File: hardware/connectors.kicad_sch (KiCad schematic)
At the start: 4 parts, among them J1 74650073R, J4 Conn_01x06, J5 UMPT-08-01-L-RA-WT-P-TR, J8 UMPT-08-01-L-RA-WT-P-TR

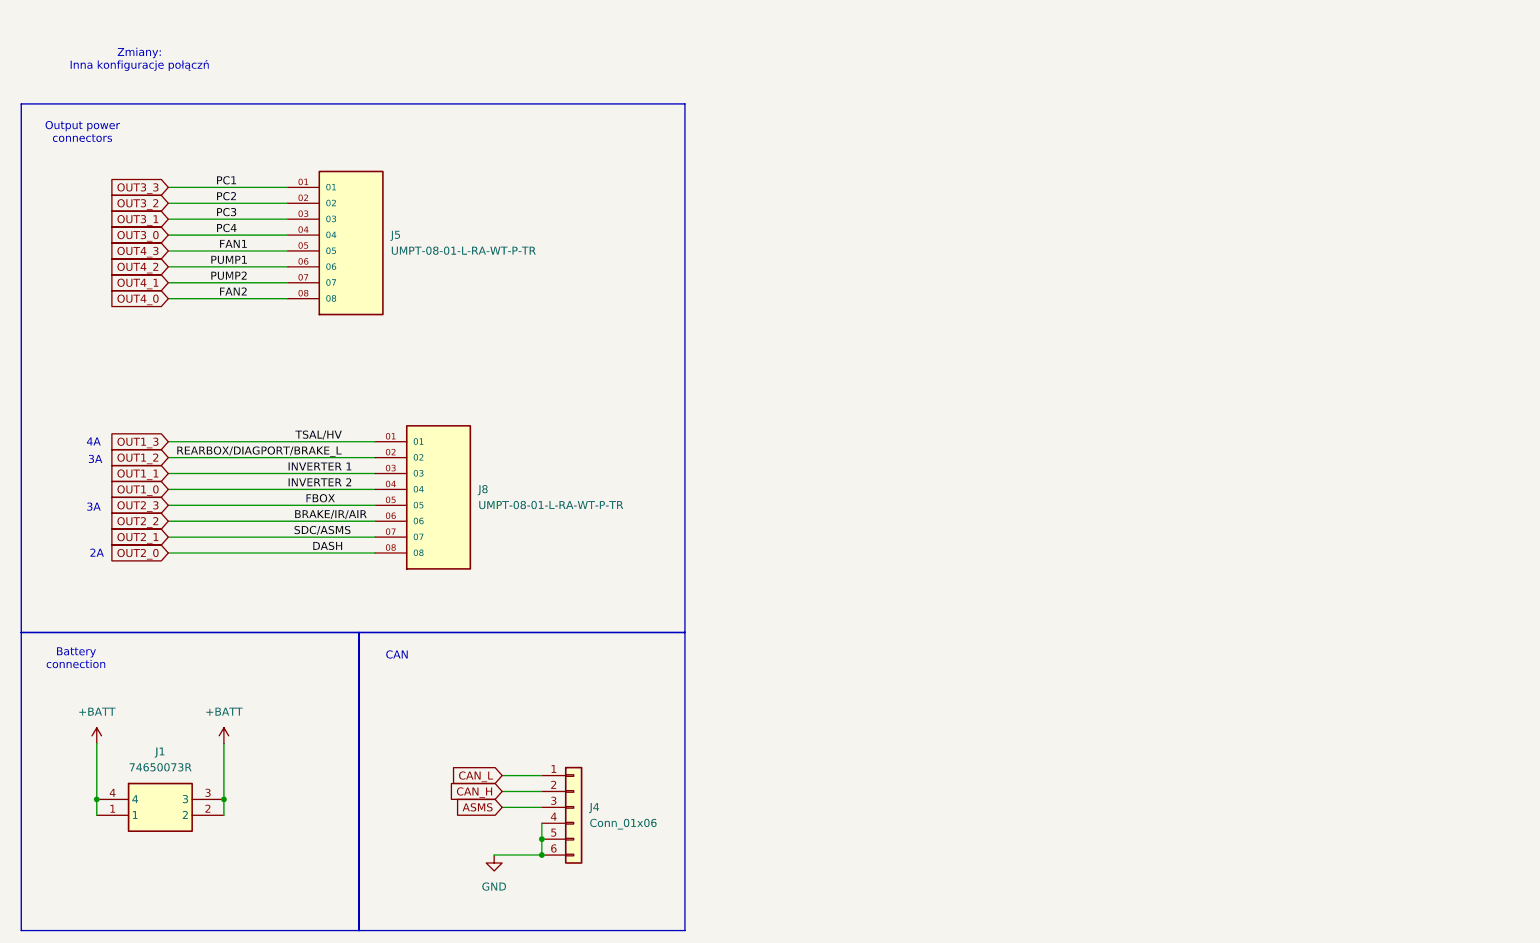
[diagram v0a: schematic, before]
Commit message: Changed CAN to isolated and added a new board-to-board plug
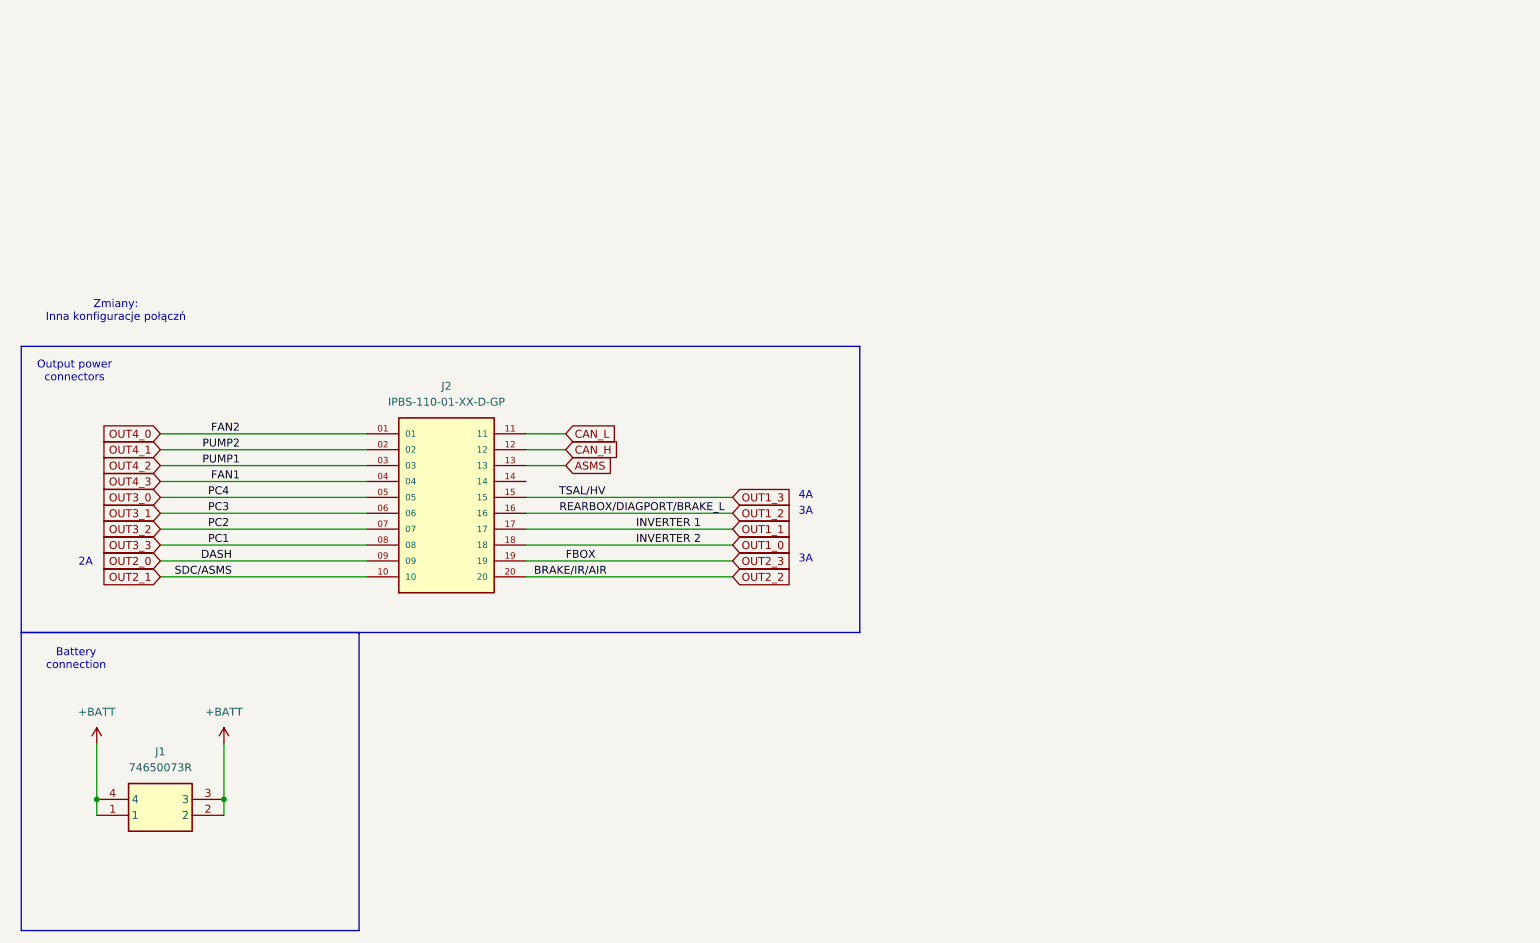
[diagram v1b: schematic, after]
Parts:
- removed J4: Conn_01x06, Connector_IDC:IDC-Header_2x03_P2.54mm_Vertical, symbol Connector_Generic:Conn_01x06
- removed J5, J8: UMPT-08-01-L-RA-WT-P-TR, UMPT-08-01-L-RA-WT-P-TR:SAMTEC_UMPT-08-01-L-RA-WT-P-TR, symbol UMPT-08-01-L-RA-WT-P-TR:UMPT-08-01-L-RA-WT-P-TR
- added J2: IPBS-110-01-XX-D-GP, IPBS-110-01-T-D-GP:SAMTEC_IPBS-110-01-XX-D-GP, symbol IPBS-110-01-XX-D-GP:IPBS-110-01-XX-D-GP
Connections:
- net ASMS: now also J2.13
- net CAN_H: now also J2.12
- net CAN_L: now also J2.11
- net OUT1_0: now also J2.18
- net OUT1_1: now also J2.17
- net OUT1_2: now also J2.16
- net OUT1_3: now also J2.15
- net OUT2_0: now also J2.09
- net OUT2_1: now also J2.10
- net OUT2_2: now also J2.20
- net OUT2_3: now also J2.19
- net OUT3_0: now also J2.05
- net OUT3_1: now also J2.06
- net OUT3_2: now also J2.07
- net OUT3_3: now also J2.08
- net OUT4_0: now also J2.01
- net OUT4_1: now also J2.02
- net OUT4_2: now also J2.03
- net OUT4_3: now also J2.04
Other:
- note removed: "CAN"

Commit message: NEW SCHEMATIC
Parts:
- added C28: 10n, Capacitor_SMD:C_0603_1608Metric_Pad1.08x0.95mm_HandSolder, symbol Device:C_Small
- added D10: PESD5V0L2BT,215, Package_TO_SOT_SMD:SOT-23-3, symbol Device:D_TVS_Dual_AAC
- added D11: SP0505BAHTG, Package_TO_SOT_SMD:SOT-23-6_Handsoldering, symbol Power_Protection:SP0505BAHT
- added J3: FTSH-107-01-L-D-K, PDM:FTSH-107-XX-YYY-D-K, symbol PDM:FTSH-107-01-L-D-K
- added J4: USB_C_Receptacle_USB2.0_14P, Connector_USB:USB_C_Receptacle_JAE_DX07S024WJ3R400, symbol Connector:USB_C_Receptacle_USB2.0_14P
- added R14, R15: 5k1, Resistor_SMD:R_0603_1608Metric_Pad0.98x0.95mm_HandSolder, symbol Device:R_Small
- added U5: TPD2E2U06DCK, Package_TO_SOT_SMD:SOT-323_SC-70, symbol Power_Protection:TPD2E2U06DCK
- J1: footprint 74650073R -> PDM:74650073R; symbol Redcube_conn:74650073R -> PDM:74650073R; Done? (none) -> y
- J2: footprint IPBS-110-01-T-D-GP:SAMTEC_IPBS-110-01-XX-D-GP -> PDM:IPBS11001TDGP; symbol IPBS-110-01-XX-D-GP:IPBS-110-01-XX-D-GP -> PDM:IPBS-110-01-T-D-GP; Done? (none) -> y; Manufacturer_Name (none) -> SAMTEC; Manufacturer_Part_Number (none) -> IPBS-110-01-T-D-GP; Mouser Part Number (none) -> 200-IPBS11001TDGP; Mouser Price/Stock (none) -> https://www.mouser.co.uk/ProductDetail/Samtec/IPBS-110-01-T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
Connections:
- net OUT1_0: now also J2.9; no longer J2.18
- net OUT1_1: now also J2.10; no longer J2.17
- net OUT1_2: now also J2.20; no longer J2.16
- net OUT1_3: now also J2.19; no longer J2.15
- net OUT2_0: now also J2.5; no longer J2.09
- net OUT2_1: now also J2.6; no longer J2.10
- net OUT2_2: now also J2.7; no longer J2.20
- net OUT2_3: now also J2.8; no longer J2.19
- net OUT3_0: now also J2.1; no longer J2.05
- net OUT3_1: now also J2.2; no longer J2.06
- net OUT3_2: now also J2.3; no longer J2.07
- net OUT3_3: now also J2.4; no longer J2.08
- net CAN_H renamed CAN.P
- net CAN.P: now also D10.2 (A2)
- net CAN_L renamed CAN.N
- net CAN.N: now also D10.1 (A1)
- removed net OUT4_0: J2.01
- removed net OUT4_1: J2.02
- removed net OUT4_2: J2.03
- removed net OUT4_3: J2.04
- new net: J4.B5 (CC2), R15.2
- new net: J4.A5 (CC1), R14.2
- new net: C28.1, J4.S1 (SHIELD)
- new net +3V3: J3.3
- new net CAN_GND_ISO: D10.3 (common)
- new net GND: C28.2, D11.2 (A), J3.11, J3.5, J3.7, J4.A1 (GND), J4.A12 (GND), J4.B1 (GND), J4.B12 (GND), R14.1, R15.1, U5.3
- new net OUT0_0: J2.18
- new net OUT0_1: J2.17
- new net OUT0_2: J2.16
- new net OUT0_3: J2.15
- new net RST: D11.4 (K), J3.12
- new net SW.CLK: D11.6 (K), J3.6
- new net SW.DIO: D11.5 (K), J3.4
- new net USART.RX: D11.1 (K), J3.13
- new net USART.TX: D11.3 (K), J3.14
- new net USB.+: J4.A6 (D+), J4.B6 (D+), U5.2
- new net USB.-: J4.A7 (D-), J4.B7 (D-), U5.1
- new net VBUS: J4.A4 (VBUS), J4.A9 (VBUS), J4.B4 (VBUS), J4.B9 (VBUS)
- no-connect marks 0 -> 6
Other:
- note added: "BATTERY CONNECTOR"
- note added: "Changes: New connection layout"
- note added: "ESD CAN PROTECTION"
- note added: "ESD PROGRAMMER PROTECTION"
- note added: "ESD USB PROTECTION"
- note added: "OUTPUT POWER CONNECTOR"
- note added: "PROGRAMMER"
- note added: "USB C"
- note removed: "Battery connection"
- note removed: "Output power connectors"
- note removed: "Zmiany: Inna konfiguracje połączń"
- company: (none) -> Authors: Grzegorz Potocki Jędrzej Kasprzyk
- title: (none) -> PDUv3
- moved on the sheet: J1, J2

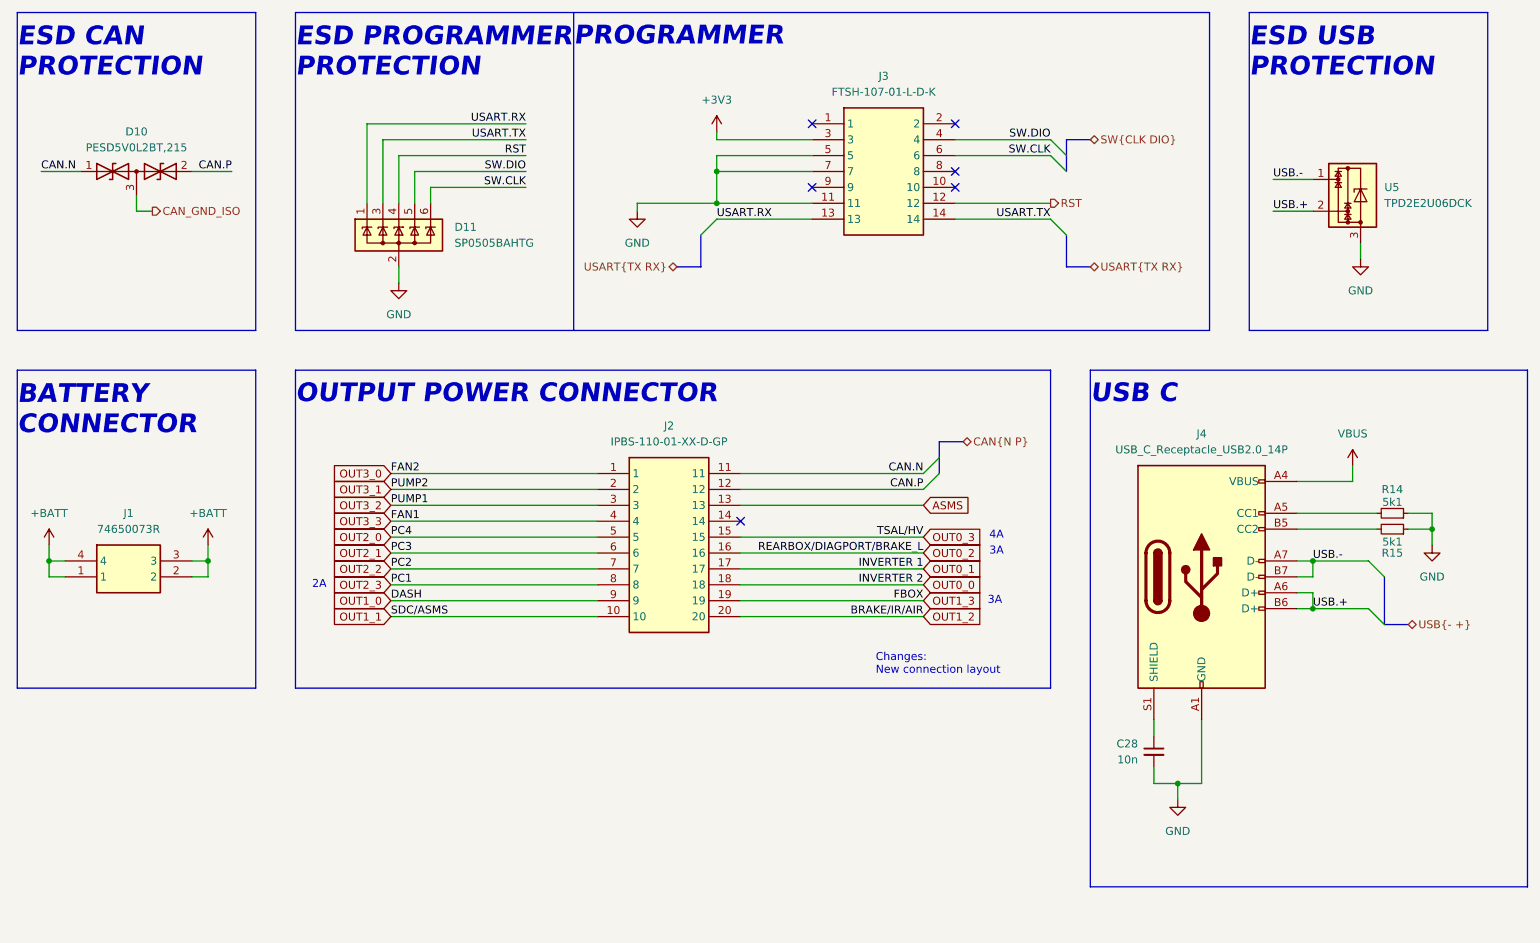
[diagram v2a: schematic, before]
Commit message: new pcb layout & can coppied from steeringwheel
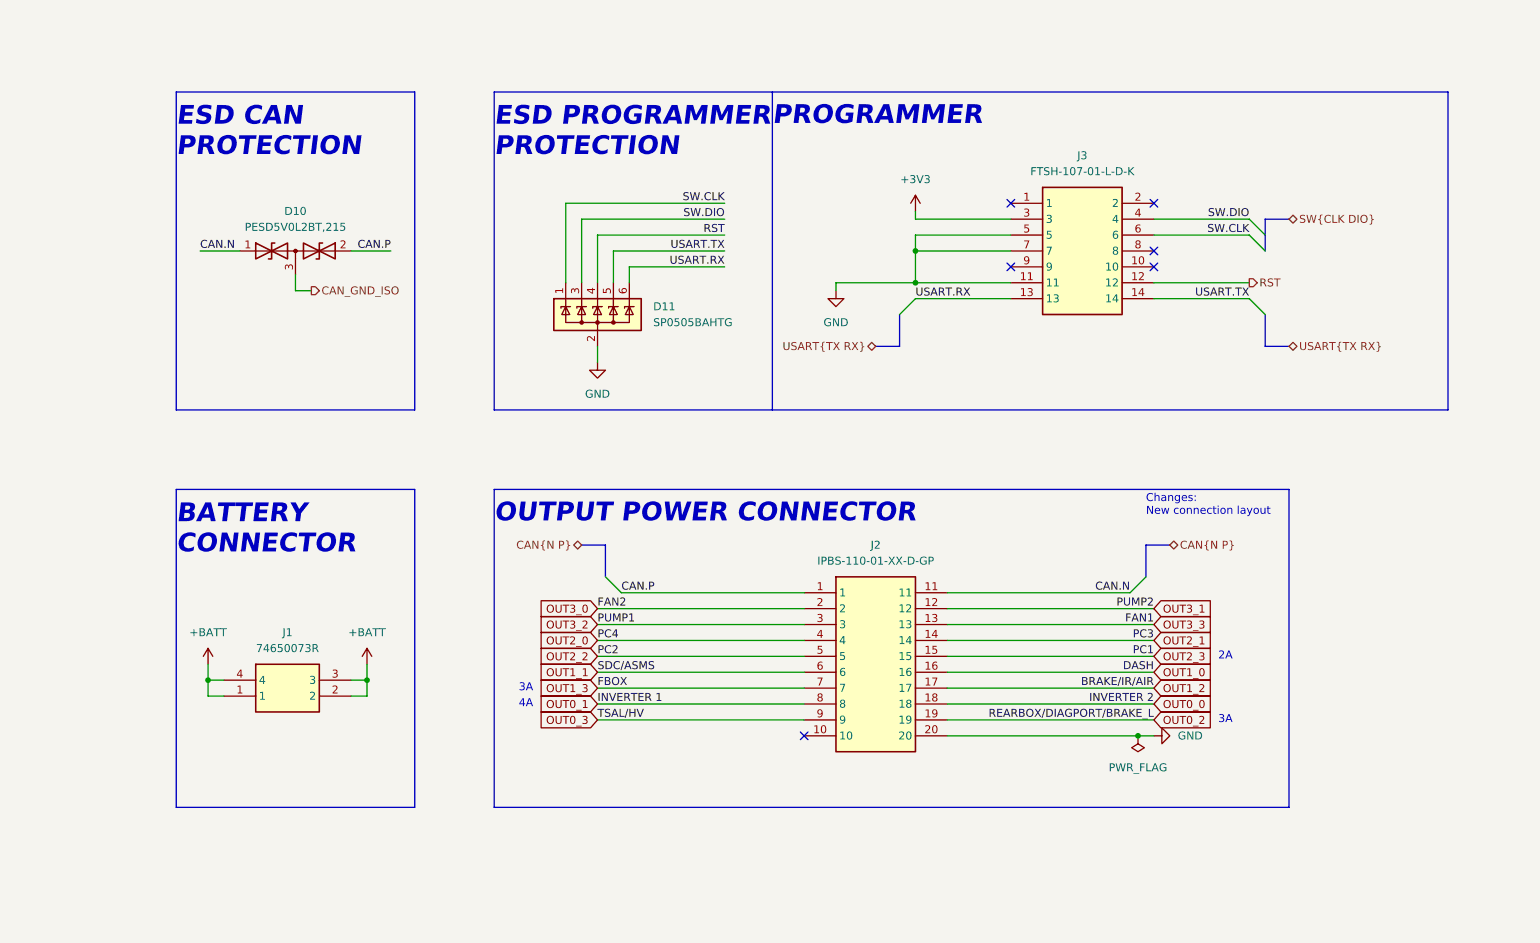
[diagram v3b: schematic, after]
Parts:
- removed C28: 10n, Capacitor_SMD:C_0603_1608Metric_Pad1.08x0.95mm_HandSolder, symbol Device:C_Small
- removed J4: USB_C_Receptacle_USB2.0_14P, Connector_USB:USB_C_Receptacle_JAE_DX07S024WJ3R400, symbol Connector:USB_C_Receptacle_USB2.0_14P
- removed R14, R15: 5k1, Resistor_SMD:R_0603_1608Metric_Pad0.98x0.95mm_HandSolder, symbol Device:R_Small
- removed U5: TPD2E2U06DCK, Package_TO_SOT_SMD:SOT-323_SC-70, symbol Power_Protection:TPD2E2U06DCK
- J2: footprint PDM:IPBS11001TDGP -> PDM:IPBT110H1TDRAGP
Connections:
- net ASMS is gone; now on net OUT3_3: J2.13
- net CAN.P: now also J2.1; no longer J2.12
- net GND: now also J2.20
- net OUT0_1: now also J2.8; no longer J2.17
- net OUT0_2: now also J2.19; no longer J2.16
- net OUT0_3: now also J2.9; no longer J2.15
- net OUT1_0: now also J2.16; no longer J2.9
- net OUT1_1: now also J2.6; no longer J2.10
- net OUT1_2: now also J2.17; no longer J2.20
- net OUT1_3: now also J2.7; no longer J2.19
- net OUT2_0: now also J2.4; no longer J2.5
- net OUT2_1: now also J2.14; no longer J2.6
- net OUT2_2: now also J2.5; no longer J2.7
- net OUT2_3: now also J2.15; no longer J2.8
- net OUT3_0: now also J2.2; no longer J2.1
- net OUT3_1: now also J2.12; no longer J2.2
- net OUT3_3: no longer J2.4
- net SW.CLK: now also D11.1 (K); no longer D11.6 (K)
- net SW.DIO: now also D11.3 (K); no longer D11.5 (K)
- net USART.RX: now also D11.6 (K); no longer D11.1 (K)
- net USART.TX: now also D11.5 (K); no longer D11.3 (K)
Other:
- note removed: "ESD USB PROTECTION"
- note removed: "USB C"
- moved on the sheet: D10, D11, J1, J3
